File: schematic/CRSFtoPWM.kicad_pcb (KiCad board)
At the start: 4 copper layers, 40 x 21 mm, 30 parts, among them J1 Bat+, J2 UART1/Rx, J3 ICSP, J4 TSW-104-08-G-T-RA, J5 TSW-104-08-G-T-RA, J6 TSW-104-08-G-T-RA, J7 TSW-102-08-L-T-RA, U1 AP7375-50W5-7, U2 AP2210N-3.3TRG1, U3 ATSAMD21E18A-MU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

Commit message: Updated schematic to correct channel numbering
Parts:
- C1, C2: value 100n -> 100nF
- C3, C6: value 10 uF -> 10uF
- C4, C5: value 1 uF -> 1uF
- C7: value 2.2 uF -> 2.2uF
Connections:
- J5 pad 1: CH2 -> CH4
- J5 pad 10: CH5 -> CH1
- J5 pad 4: CH1 -> CH3
- J5 pad 7: CH6 -> CH2
- J6 pad 10: CH3 -> CH5
- J6 pad 7: CH4 -> CH6
- U3 pad 11: CH1 -> CH3
- U3 pad 12: CH2 -> CH4
- U3 pad 13: CH3 -> CH5
- U3 pad 14: CH4 -> CH6
- U3 pad 7: CH5 -> CH1
- U3 pad 8: CH6 -> CH2
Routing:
- net CH5: track 12.3 -> 8.58 mm
- net CH1: track 9.14 -> 12.3 mm
- net CH2: track 8.30 -> 10.8 mm
- net CH4: track 9.86 -> 8.30 mm
- net CH6: track 10.8 -> 9.86 mm
- net CH3: track 8.58 -> 9.14 mm

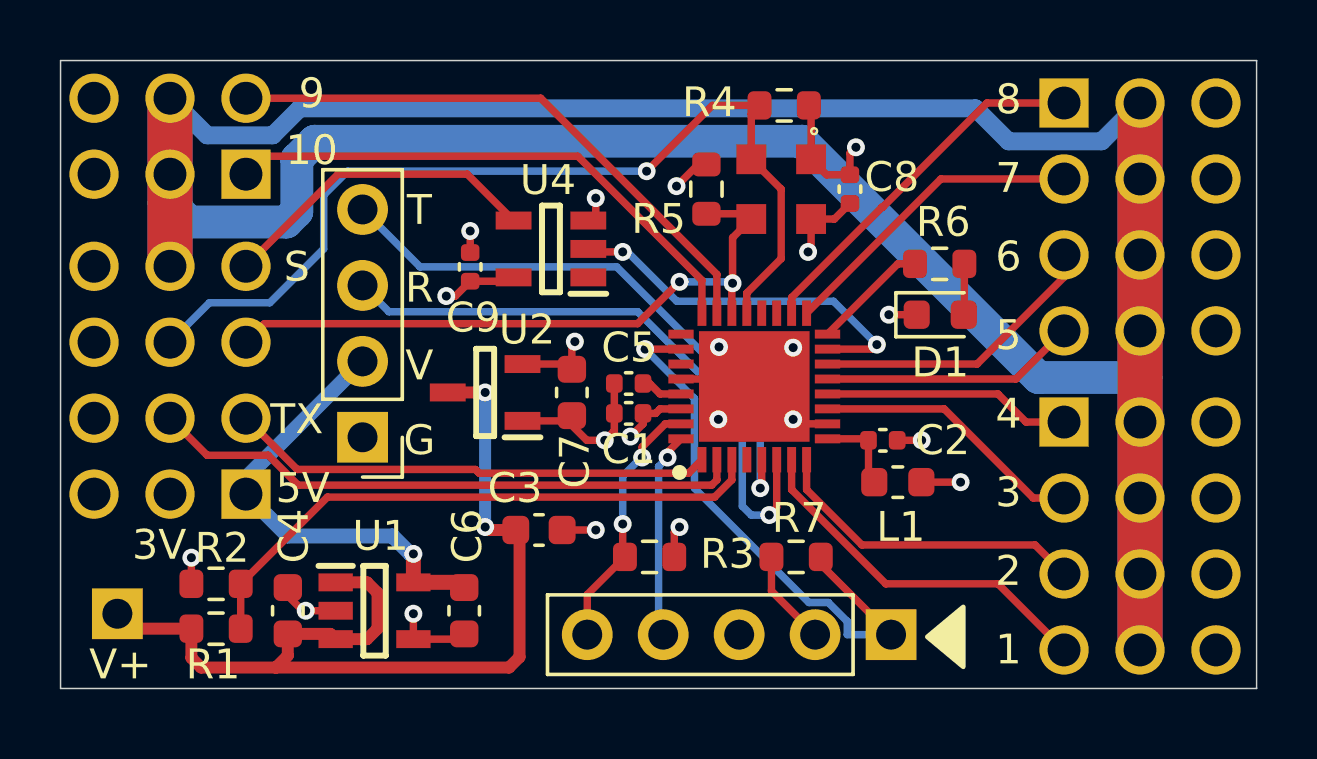
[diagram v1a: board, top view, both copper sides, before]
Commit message: Changed power circuit
3.3V regulator now uses regulated 5V for input.  Less load on 3.3V regulator and only the 5V regulator has high voltage input.
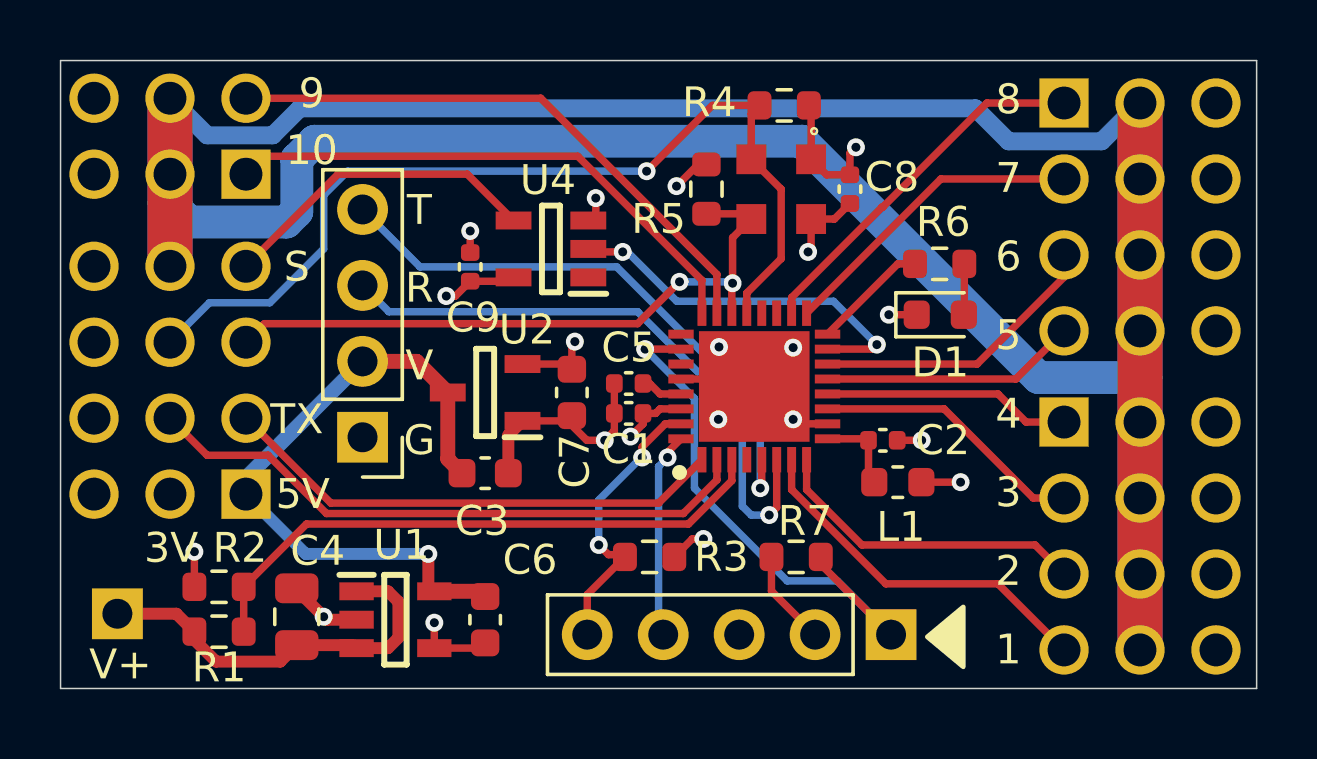
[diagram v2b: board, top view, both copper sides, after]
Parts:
- C4: footprint Capacitor_SMD:C_0603_1608Metric -> Capacitor_SMD:C_0805_2012Metric
- moved C3 2.62 mm to (155.2, 108.4)
- moved C6 0.76 mm to (155.2, 113.3)
- moved U1 0.76 mm to (152.2, 113.3)
- moved C4 0.36 mm to (148.9, 113.2)
- moved R1 0.14 mm to (146.3, 113.7)
- moved R2 0.14 mm to (146.3, 112.2)
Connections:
- C3 pad 1: Vbat -> +5V
- U2 pad 3: Vbat -> +5V
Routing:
- net Vbat: track 32.4 -> 13.0 mm, vias 2 -> 0
- net +5V: track 14.4 -> 21.5 mm
- net GND: track 20.2 -> 21.9 mm, vias 14 -> 13
- net Net-(J3-Pad5): track 8.63 -> 9.57 mm
- net TX2: track 16.2 -> 17.0 mm
- net RX2: track 20.0 -> 20.8 mm
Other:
- board text added: "V1.1 QES 2023"
- board text removed: "V1.0 QES 2023"

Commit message: Changed input cap back to 0603 and new gerbers
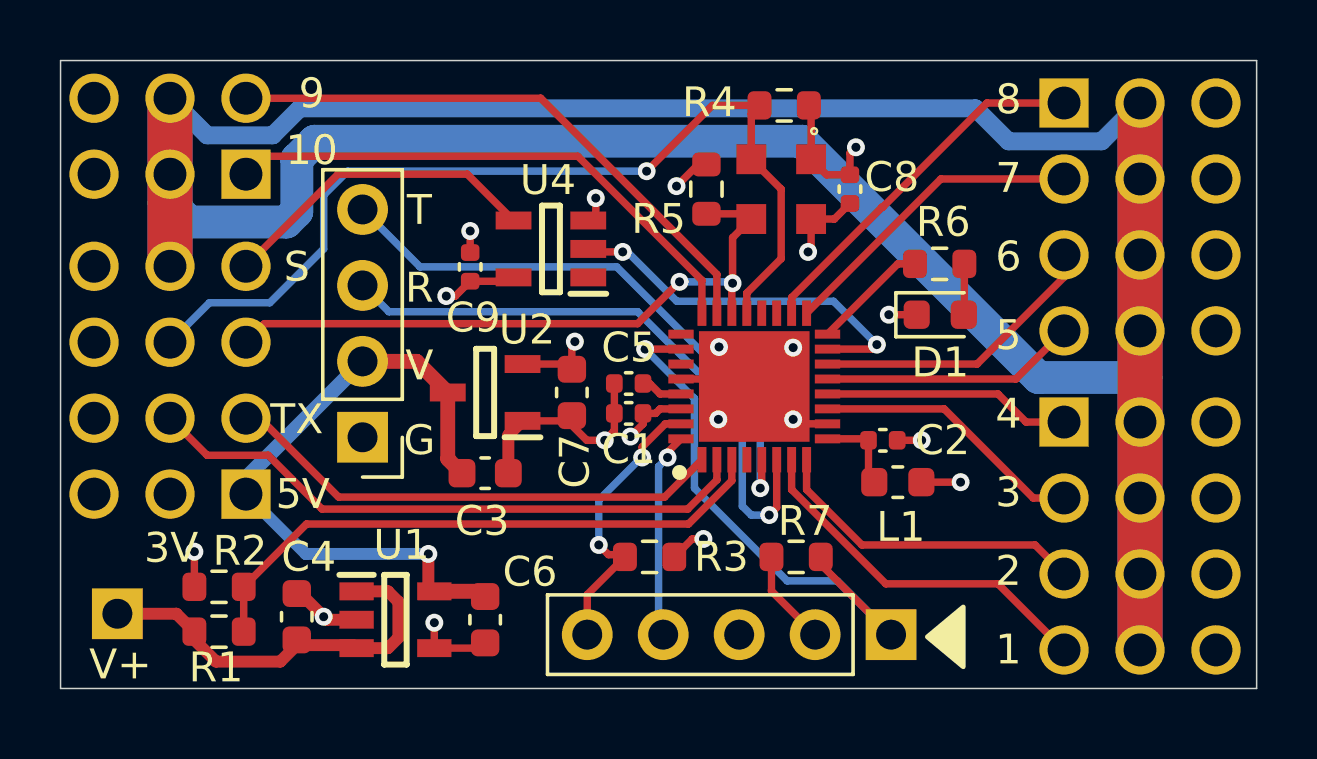
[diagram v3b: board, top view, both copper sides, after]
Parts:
- C4: footprint Capacitor_SMD:C_0805_2012Metric -> Capacitor_SMD:C_0603_1608Metric
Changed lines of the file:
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@@
     (property "Sheetname" "")
     (attr smd)
-    (fp_text reference "R1" (at 0 1.2) (layer "F.SilkS")
+    (fp_text reference "R1" (at -0.1 1.2) (layer "F.SilkS")
       (effects (font (size 1 1) (thickness 0.15)))
     )
@@
     )
   )
-  (footprint "Capacitor_SMD:C_0805_2012Metric" (layer "F.Cu")
+  (footprint "Capacitor_SMD:C_0603_1608Metric" (layer "F.Cu")
     (at 148.9 113.2 90)
-    (descr "Capacitor SMD 0805 (2012 Metric), square (rectangular) end terminal, IPC_7351 nominal, (Body size source: IPC-SM-782 page 76, https://www.pcb-3d.com/wordpress/wp-content/uploads/ipc-sm-782a_amendment_1_and_2.pdf, https://docs.google.com/spreadsheets/d/1BsfQQcO9C6DZCsRaXUlFlo91Tg2WpOkGARC1WS5S8t0/edit?usp=sharing), generated with kicad-footprint-generator")
+    (descr "Capacitor SMD 0603 (1608 Metric), square (rectangular) end terminal, IPC_7351 nominal, (Body size source: IPC-SM-782 page 76, https://www.pcb-3d.com/wordpress/wp-content/uploads/ipc-sm-782a_amendment_1_and_2.pdf), generated with kicad-footprint-generator")
     (tags "capacitor")
     (property "Sheetfile" "CRSFtoPWM.kicad_sch")
     (property "Sheetname" "")
     (attr smd)
-    (fp_text reference "C4" (at 2.2 0.7 180) (layer "F.SilkS")
-      (effects (font (size 1 1) (thickness 0.15)))
-    )
-    (fp_text value "1uF" (at 0 1.68 90) (layer "F.Fab")
+    (fp_text reference "C4" (at 2 0.4 180) (layer "F.SilkS")
+      (effects (font (size 1 1) (thickness 0.15)))
+    )
+    (fp_text value "1uF" (at 0 1.43 90) (layer "F.Fab")
       (effects (font (size 1 1) (thickness 0.15)))
     )
     (fp_text user "${REFERENCE}" (at 0 0 90) (layer "F.Fab")
-      (effects (font (size 0.5 0.5) (thickness 0.08)))
-    )
-    (fp_line (start -0.261252 -0.735) (end 0.261252 -0.735) (layer "F.SilkS") (width 0.12))
-    (fp_line (start -0.261252 0.735) (end 0.261252 0.735) (layer "F.SilkS") (width 0.12))
-    (fp_line (start 1.7 0.98) (end -1.7 0.98) (layer "F.CrtYd") (width 0.05))
-    (fp_line (start -1.7 -0.98) (end 1.7 -0.98) (layer "F.CrtYd") (width 0.05))
-    (fp_line (start 1.7 -0.98) (end 1.7 0.98) (layer "F.CrtYd") (width 0.05))
-    (fp_line (start -1.7 0.98) (end -1.7 -0.98) (layer "F.CrtYd") (width 0.05))
-    (fp_line (start 1 -0.625) (end 1 0.625) (layer "F.Fab") (width 0.1))
-    (fp_line (start -1 0.625) (end -1 -0.625) (layer "F.Fab") (width 0.1))
-    (fp_line (start -1 -0.625) (end 1 -0.625) (layer "F.Fab") (width 0.1))
-    (fp_line (start 1 0.625) (end -1 0.625) (layer "F.Fab") (width 0.1))
-    (pad "1" smd roundrect (at -0.95 0 90) (size 1 1.45) (layers "F.Cu" "F.Paste" "F.Mask") (roundrect_rratio 0.25)
+      (effects (font (size 0.4 0.4) (thickness 0.06)))
+    )
+    (fp_line (start -0.14058 -0.51) (end 0.14058 -0.51) (layer "F.SilkS") (width 0.12))
+    (fp_line (start -0.14058 0.51) (end 0.14058 0.51) (layer "F.SilkS") (width 0.12))
+    (fp_line (start -1.48 -0.73) (end 1.48 -0.73) (layer "F.CrtYd") (width 0.05))
+    (fp_line (start 1.48 -0.73) (end 1.48 0.73) (layer "F.CrtYd") (width 0.05))
+    (fp_line (start 1.48 0.73) (end -1.48 0.73) (layer "F.CrtYd") (width 0.05))
+    (fp_line (start -1.48 0.73) (end -1.48 -0.73) (layer "F.CrtYd") (width 0.05))
+    (fp_line (start 0.8 0.4) (end -0.8 0.4) (layer "F.Fab") (width 0.1))
+    (fp_line (start -0.8 0.4) (end -0.8 -0.4) (layer "F.Fab") (width 0.1))
+    (fp_line (start 0.8 -0.4) (end 0.8 0.4) (layer "F.Fab") (width 0.1))
+    (fp_line (start -0.8 -0.4) (end 0.8 -0.4) (layer "F.Fab") (width 0.1))
+    (pad "1" smd roundrect (at -0.775 0 90) (size 0.9 0.95) (layers "F.Cu" "F.Paste" "F.Mask") (roundrect_rratio 0.25)
       (net 3 "Vbat") (pintype "passive"))
-    (pad "2" smd roundrect (at 0.95 0 90) (size 1 1.45) (layers "F.Cu" "F.Paste" "F.Mask") (roundrect_rratio 0.25)
+    (pad "2" smd roundrect (at 0.775 0 90) (size 0.9 0.95) (layers "F.Cu" "F.Paste" "F.Mask") (roundrect_rratio 0.25)
       (net 30 "GND") (pintype "passive"))
-    (model "${KICAD6_3DMODEL_DIR}/Capacitor_SMD.3dshapes/C_0805_2012Metric.wrl"
+    (model "${KICAD6_3DMODEL_DIR}/Capacitor_SMD.3dshapes/C_0603_1608Metric.wrl"
       (offset (xyz 0 0 0))
       (scale (xyz 1 1 1))
@@
     (property "Sheetname" "")
     (attr smd)
-    (fp_text reference "C6" (at -2 -1.5 180) (layer "F.SilkS")
+    (fp_text reference "C6" (at -1.6 -1.5 180) (layer "F.SilkS")
       (effects (font (size 1 1) (thickness 0.15)))
     )
@@
     (property "Sheetname" "")
     (attr smd)
-    (fp_text reference "R2" (at -0.7 1.3) (layer "F.SilkS")
+    (fp_text reference "R2" (at -0.7 1.2) (layer "F.SilkS")
       (effects (font (size 1 1) (thickness 0.15)))
     )
@@
   (segment (start 147.2 101.48) (end 150.28 98.4) (width 0.25) (layer "F.Cu") (net 31))
   (segment (start 154.6 98.4) (end 156.15 99.95) (width 0.25) (layer "F.Cu") (net 31))
-  (segment (start 147.2 106.56) (end 150.04 109.4) (width 0.25) (layer "F.Cu") (net 32))
-  (segment (start 161 109.4) (end 162.45 107.95) (width 0.25) (layer "F.Cu") (net 32))
-  (segment (start 150.04 109.4) (end 161 109.4) (width 0.25) (layer "F.Cu") (net 32))
-  (segment (start 149.895232 109.749501) (end 161.825499 109.749501) (width 0.25) (layer "F.Cu") (net 33))
-  (segment (start 161.825499 109.749501) (end 162.95 108.625) (width 0.25) (layer "F.Cu") (net 33))
-  (segment (start 147.94573 107.8) (end 149.895232 109.749501) (width 0.25) (layer "F.Cu") (net 33))
+  (segment (start 161.2 109.2) (end 162.45 107.95) (width 0.25) (layer "F.Cu") (net 32))
+  (segment (start 147.2 106.56) (end 147.66 106.56) (width 0.25) (layer "F.Cu") (net 32))
+  (segment (start 147.66 106.56) (end 150.3 109.2) (width 0.25) (layer "F.Cu") (net 32))
+  (segment (start 150.3 109.2) (end 161.2 109.2) (width 0.25) (layer "F.Cu") (net 32))
+  (segment (start 145.9 107.8) (end 147.94573 107.8) (width 0.25) (layer "F.Cu") (net 33))
+  (segment (start 149.74573 109.6) (end 161.975 109.6) (width 0.25) (layer "F.Cu") (net 33))
+  (segment (start 147.94573 107.8) (end 149.74573 109.6) (width 0.25) (layer "F.Cu") (net 33))
+  (segment (start 162.95 108.625) (end 162.95 107.95) (width 0.25) (layer "F.Cu") (net 33))
+  (segment (start 161.975 109.6) (end 162.95 108.625) (width 0.25) (layer "F.Cu") (net 33))
   (segment (start 144.66 106.56) (end 145.9 107.8) (width 0.25) (layer "F.Cu") (net 33))
-  (segment (start 145.9 107.8) (end 147.94573 107.8) (width 0.25) (layer "F.Cu") (net 33))
-  (segment (start 162.95 108.625) (end 162.95 107.95) (width 0.25) (layer "F.Cu") (net 33))
   (segment (start 164.1 96.375) (end 164.375 96.1) (width 0.25) (layer "F.Cu") (net 34))
   (segment (start 163.95 103.05) (end 163.95 102.375) (width 0.25) (layer "F.Cu") (net 34))
